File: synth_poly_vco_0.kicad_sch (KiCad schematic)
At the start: 44 parts, among them J1 cv_in, J2 out_pulse, J3 Power, J4 out_saw, J5 out_triangle, Q1 BC558, Q2 BC548, U1 40106, U2 TL074, U3 TL072

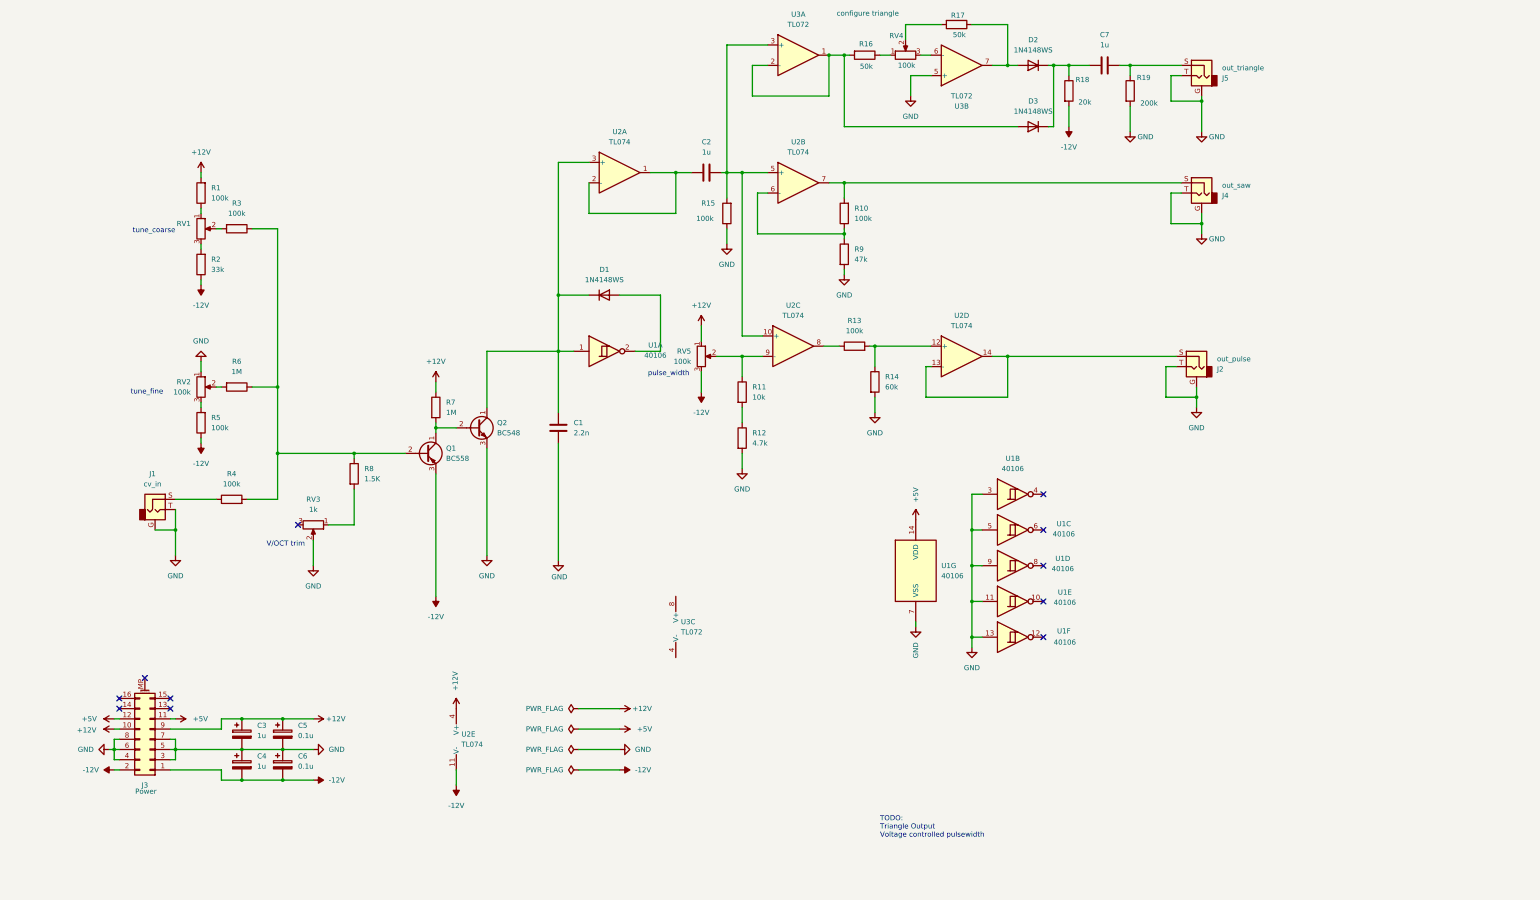
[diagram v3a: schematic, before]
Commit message: Add - power supply filtering - reverse voltage protection - test points
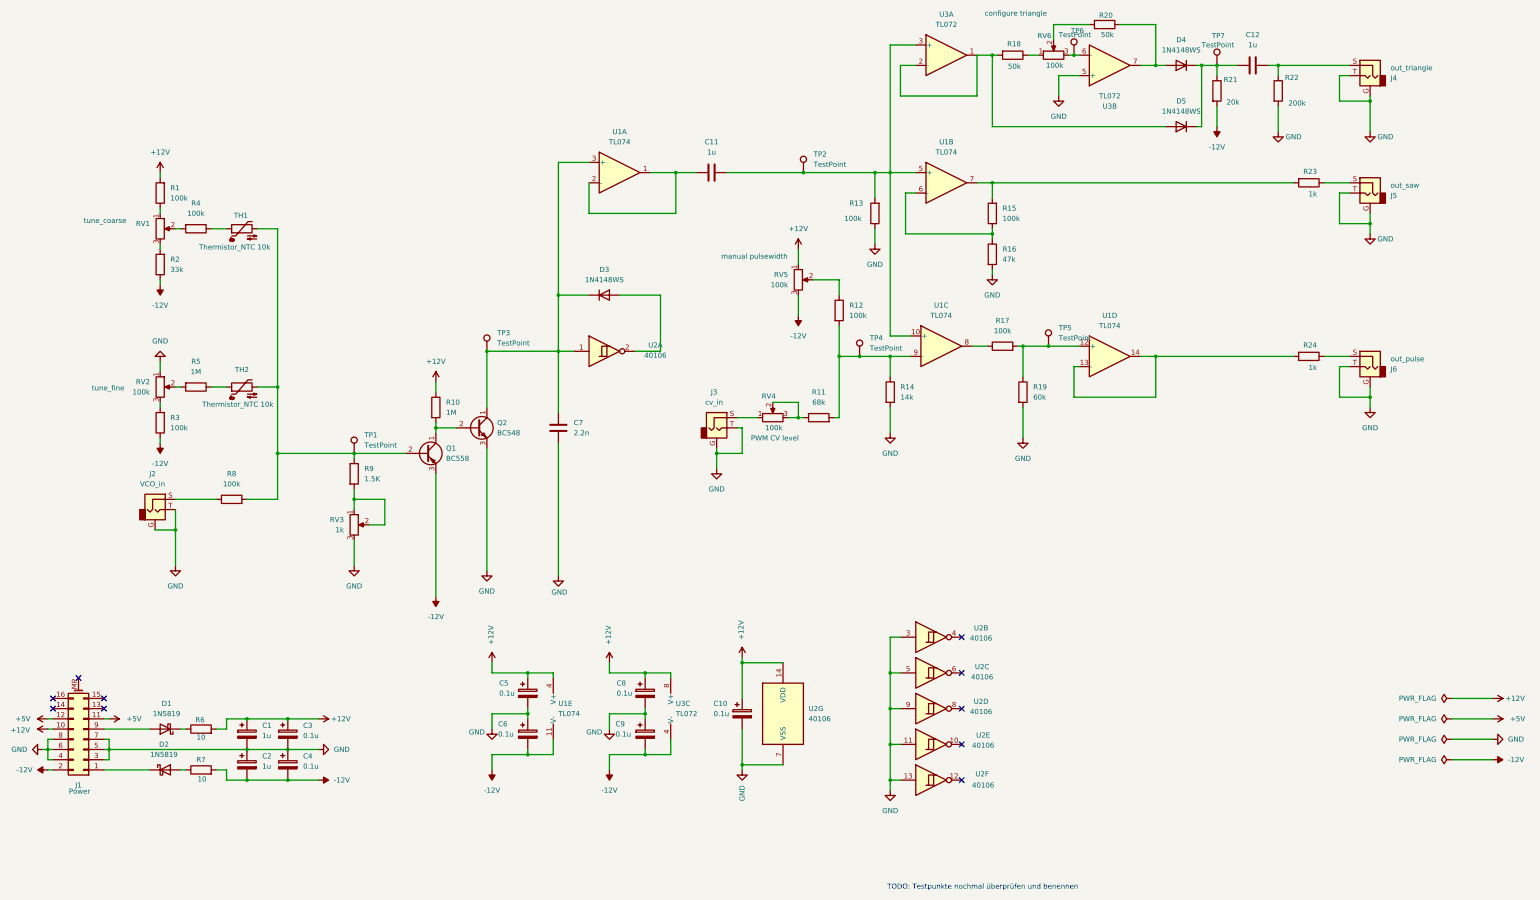
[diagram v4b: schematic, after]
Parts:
- added C10, C5, C6, C8, C9: 0.1u, symbol Device:C_Polarized
- added D1, D2: 1N5819, Diode_THT:D_DO-41_SOD81_P10.16mm_Horizontal, symbol Diode:1N5819
- added J3: cv_in, symbol Connector_Audio:AudioJack2_Ground
- added R11: 68k, symbol Device:R
- added R23, R24: 1k, symbol Device:R
- added R6, R7: 10, symbol Device:R
- added RV4: 100k, symbol Device:R_Potentiometer
- added TH1, TH2: Thermistor_NTC 10k, symbol Device:Thermistor_NTC
- added TP1, TP2, TP3, TP4, TP5, TP6, TP7: TestPoint, symbol Connector:TestPoint
- J2: renamed from J1; value cv_in -> VCO_in
- R12: value 4.7k -> 100k
- R14: renamed from R11; value 10k -> 14k
- renumbered C3 to C1, C2 to C11, C7 to C12, C4 to C2, C5 to C3, C6 to C4, C1 to C7, D1 to D3, D2 to D4, D3 to D5, J3 to J1, J5 to J4, J4 to J5, J2 to J6, R7 to R10, R15 to R13, R10 to R15, R9 to R16, R13 to R17, R16 to R18, R14 to R19, R17 to R20, R18 to R21, R19 to R22, R5 to R3, R3 to R4, R6 to R5, R4 to R8, R8 to R9, RV4 to RV6, U2 to U1, U1 to U2
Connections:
- net +12V: now also U2.14 (VDD), U3.8 (V+), C10.1, C5.1, C8.1, R6.2; no longer J1.9 (Pin_9)
- net +5V: no longer U2.14 (VDD)
- net -12V: now also U3.4 (V-), C6.2, C9.2, R7.2; no longer J1.1 (Pin_1)
- net GND: now also R14.2, RV3.3, C10.2, C5.2, C6.1, C8.2, C9.1, J3.G, J3.T; no longer R12.2, RV3.2
- net at Q1.2 (B), R8.2, R9.1: now also TH1.2, TH2.2, TP1.1; no longer R4.1, R5.1
- net at C12.1, D4.1 (K), D5.1 (K)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: now also TP7.1
- net at R15.2, U1.7: now also R23.2; no longer J5.S
- net at C7.1, D3.1 (K), Q2.1 (C)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: now also TP3.1
- net at R12.1: now also RV5.2; no longer R14.2
- net at C11.2, R13.2, U1.10 (+)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: now also TP2.1
- net at R14.1, U1.9 (-): now also R12.2, R11.2, TP4.1; no longer RV5.2
- net at R17.2, R19.1, U1.12 (+): now also TP5.1
- net at U1.13 (-), U1.14: now also R24.2; no longer J6.S
- net at RV6.3, U3.6 (-): now also TP6.1
- net at R9.2, RV3.1: now also RV3.2
- new net: D2.1 (K), J1.1 (Pin_1)
- new net: D2.2 (A), R7.1
- new net: J5.S, R23.1
- new net: R4.1, TH1.1
- new net: D1.1 (K), R6.1
- new net: D1.2 (A), J1.9 (Pin_9)
- new net: J3.S, RV4.1
- new net: R11.1, RV4.2, RV4.3
- new net: R5.1, TH2.1
- new net: J6.S, R24.1
- no-connect marks 11 -> 10
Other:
- note added: "TODO: Testpunkte nochmal überprüfen und benennen"
- note removed: "TODO: Triangle Output Voltage controlled pulsewidth"
- note removed: "V/OCT trim"
- note removed: "pulse_width"
- note removed: "tune_coarse"
- note removed: "tune_fine"
- moved on the sheet: C1, C11, C12, C2, C3, C4, D4, D5, J1, J4, J5, J6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

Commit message: assigned footprints
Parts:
- C1, C12, C2, C3, C4, C5, C6, C7, C8, C9: footprint (none) -> Capacitor_THT:CP_Radial_D6.3mm_P2.50mm
- C10: renamed from C11; footprint (none) -> Capacitor_THT:CP_Radial_D6.3mm_P2.50mm
- C11: renamed from C10; footprint (none) -> Capacitor_THT:CP_Radial_D6.3mm_P2.50mm
- J1: footprint (none) -> Connector_IDC:IDC-Header_2x07-1MP_P2.54mm_Latch_Vertical
- J2, J3, J4, J5, J6: footprint (none) -> Connector_PinHeader_2.54mm:PinHeader_1x03_P2.54mm_Vertical
- R1, R10, R11, R12, R13, R14, R15, R16, R17, R18, R19, R2, R20, R21, R22, R23, R24, R3, R4, R5, R6, R7, R8, R9: footprint (none) -> Resistor_THT:R_Axial_DIN0204_L3.6mm_D1.6mm_P7.62mm_Horizontal
- RV1: value tune_coarse -> 100k; footprint (none) -> Potentiometer_THT:Potentiometer_Bourns_3266Y_Vertical
- RV2, RV3, RV4, RV5, RV6: footprint (none) -> Potentiometer_THT:Potentiometer_Bourns_3266Y_Vertical
- TH1, TH2: footprint (none) -> Resistor_THT:R_Axial_DIN0204_L3.6mm_D1.6mm_P2.54mm_Vertical
- TP1, TP4, TP5, TP6, TP7: footprint (none) -> TestPoint:TestPoint_Pad_D1.5mm
- TP2: renamed from TP3; footprint (none) -> TestPoint:TestPoint_Pad_D1.5mm
- TP3: renamed from TP2; footprint (none) -> TestPoint:TestPoint_Pad_D1.5mm
- U1, U2, U3: footprint (none) -> Package_DIP:DIP-14_W7.62mm_Socket

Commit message: pcb layout
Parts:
- removed J2: VCO_in, Connector_PinHeader_2.54mm:PinHeader_1x03_P2.54mm_Vertical, symbol Connector_Audio:AudioJack2_Ground
- removed J3: cv_in, Connector_PinHeader_2.54mm:PinHeader_1x03_P2.54mm_Vertical, symbol Connector_Audio:AudioJack2_Ground
- removed J4: out_triangle, Connector_PinHeader_2.54mm:PinHeader_1x03_P2.54mm_Vertical, symbol Connector_Audio:AudioJack2_Ground
- removed J5: out_saw, Connector_PinHeader_2.54mm:PinHeader_1x03_P2.54mm_Vertical, symbol Connector_Audio:AudioJack2_Ground
- removed J6: out_pulse, Connector_PinHeader_2.54mm:PinHeader_1x03_P2.54mm_Vertical, symbol Connector_Audio:AudioJack2_Ground
- added J2: IN_vco, Connector_PinHeader_2.54mm:PinHeader_1x02_P2.54mm_Vertical, symbol Connector:Conn_01x02_Pin
- added J3: Conn_01x02_Pin, Connector_PinHeader_2.54mm:PinHeader_1x02_P2.54mm_Vertical, symbol Connector:Conn_01x02_Pin
- added J4: OUT_triangle, Connector_PinHeader_2.54mm:PinHeader_1x02_P2.54mm_Vertical, symbol Connector:Conn_01x02_Pin
- added J5: OUT_saw, Connector_PinHeader_2.54mm:PinHeader_1x02_P2.54mm_Vertical, symbol Connector:Conn_01x02_Pin
- added J6: OUT_pwm, Connector_PinHeader_2.54mm:PinHeader_1x02_P2.54mm_Vertical, symbol Connector:Conn_01x02_Pin
- TH1, TH2: value Thermistor_NTC 10k -> NTC 10k
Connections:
- net +12V: no longer J1.10 (Pin_10)
- net -12V: no longer J1.2 (Pin_2)
- net GND: now also J2.2 (Pin_2), J3.2 (Pin_2), J4.2 (Pin_2), J5.2 (Pin_2), J6.2 (Pin_2)
- net at D2.1 (K), J1.1 (Pin_1): now also J1.2 (Pin_2)
- net at R8.1: now also J2.1 (Pin_1)
- net at R23.1: now also J5.1 (Pin_1)
- net at C12.2, R22.1: now also J4.1 (Pin_1)
- net at D1.2 (A), J1.9 (Pin_9): now also J1.10 (Pin_10)
- net at RV4.1: now also J3.1 (Pin_1)
- net at R24.1: now also J6.1 (Pin_1)

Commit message: modify icd optimized paths add descriptions to in and outputs
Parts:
- removed D3, D4, D5: 1N4148WS, Diode_SMD:D_SOD-323, symbol Diode:1N4148WS
- removed J1: Power, Connector_IDC:IDC-Header_2x07-1MP_P2.54mm_Latch_Vertical, symbol Connector_Generic_MountingPin:Conn_02x08_Odd_Even_MountingPin
- removed TP7: TestPoint, TestPoint:TestPoint_Pad_D1.5mm, symbol Connector:TestPoint
- added D3, D4, D5: 1N4148, Diode_THT:D_DO-35_SOD27_P7.62mm_Horizontal, symbol Diode:1N4148
- added J1: Conn_02x08_Odd_Even, Connector_IDC:IDC-Header_2x08_P2.54mm_Vertical, symbol Connector_Generic:Conn_02x08_Odd_Even
- added TP1, TP11, TP2, TP3, TP4: Test Point, TestPoint:TestPoint_Pad_D1.5mm, symbol Connector:TestPoint
- TP10: renamed from TP4; value TestPoint -> Test Point
- TP5, TP6: value TestPoint -> Test Point
- TP7: renamed from TP1; value TestPoint -> Test Point
- U3: footprint Package_DIP:DIP-14_W7.62mm_Socket -> Package_DIP:DIP-8_W7.62mm_Socket
- renumbered R13 to R11, R11 to R12, R12 to R13, TP2 to TP8, TP3 to TP9
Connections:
- net +12V: now also TP4.1
- net +5V: now also J1.11 (Pin_11), J1.12 (Pin_12), TP3.1
- net -12V: now also TP6.1
- net GND: now also TP5.1, J1.3 (Pin_3), J1.4 (Pin_4), J1.5 (Pin_5), J1.6 (Pin_6), J1.7 (Pin_7), J1.8 (Pin_8)
- net -12V_raw: now reaches D2.1 (K)
- net -12V_raw: now also J1.1 (Pin_1), J1.2 (Pin_2)
- net at C7.1, Q2.1 (C), TP8.1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: now also D3.1 (K)
- net at C12.1, R21.1: now also D4.1 (K), D5.1 (K)
- net at R20.1, U3.7: now also D4.2 (A)
- net at U2.2: now also D3.2 (A)
- net +12V_raw: now reaches D1.2 (A)
- net +12V_raw: now also J1.10 (Pin_10), J1.9 (Pin_9)
- net at R17.2, R19.1, U1.12 (+): no longer TP5.1
- net at R18.2, U3.1, U3.2 (-): now also D5.2 (A)
- net at RV6.3, U3.6 (-): now also TP11.1; no longer TP6.1
- new net CV: J1.13 (Pin_13), J1.14 (Pin_14), TP2.1
- new net Gate: J1.15 (Pin_15), J1.16 (Pin_16), TP1.1
- no-connect marks 10 -> 5
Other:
- moved on the sheet: C1, C2, C3, C4, D1, D2, R11, R20, R6, R7, TP7
